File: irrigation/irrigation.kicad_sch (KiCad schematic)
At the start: 35 parts, among them J1 Power, J10 Power, J11 Power, J12 Power, J13 Power, J14 Power, J15 Power, J2 Power, J3 Power, J4 Power, J5 Power, J6 Power, J7 24V Jmp, J8 0V Jmp, J9 Power, K1 PLC-RPT-24DC/21, K2 PLC-RPT-24DC/21, M1 Pump, SW1 25% Full, SW2 50% Full, SW3 75% Full, SW4 100% Full, SW5 Well Empty, U1 MPPT-Charger

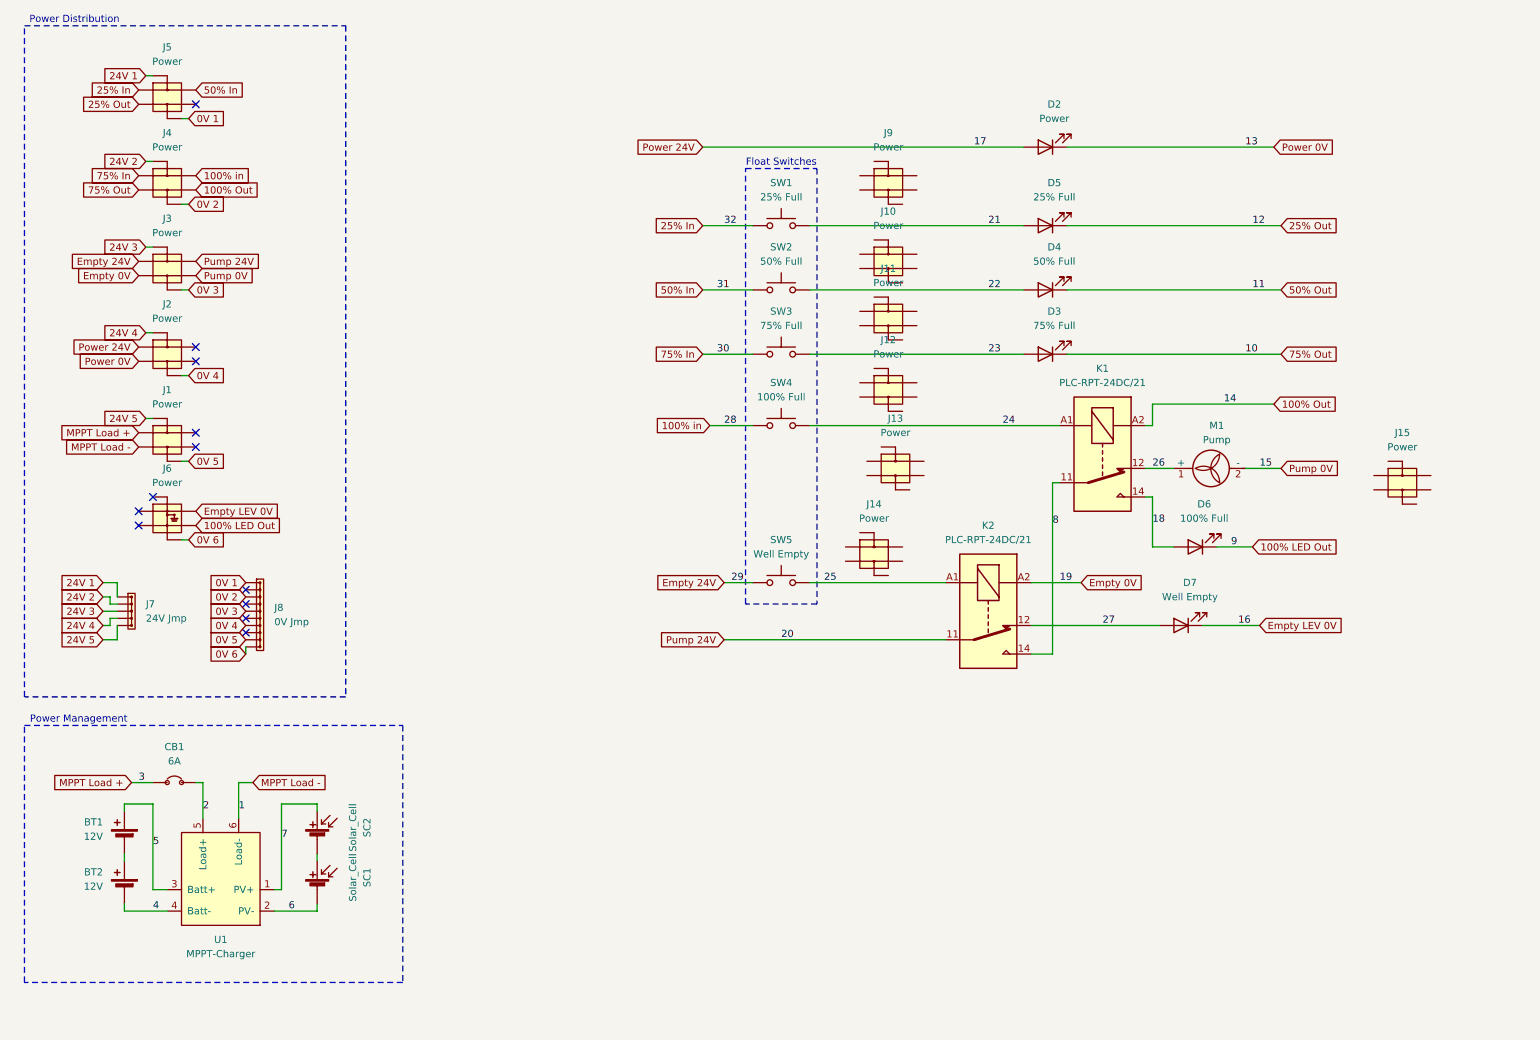
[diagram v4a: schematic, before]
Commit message: Added all the new terminal blocks
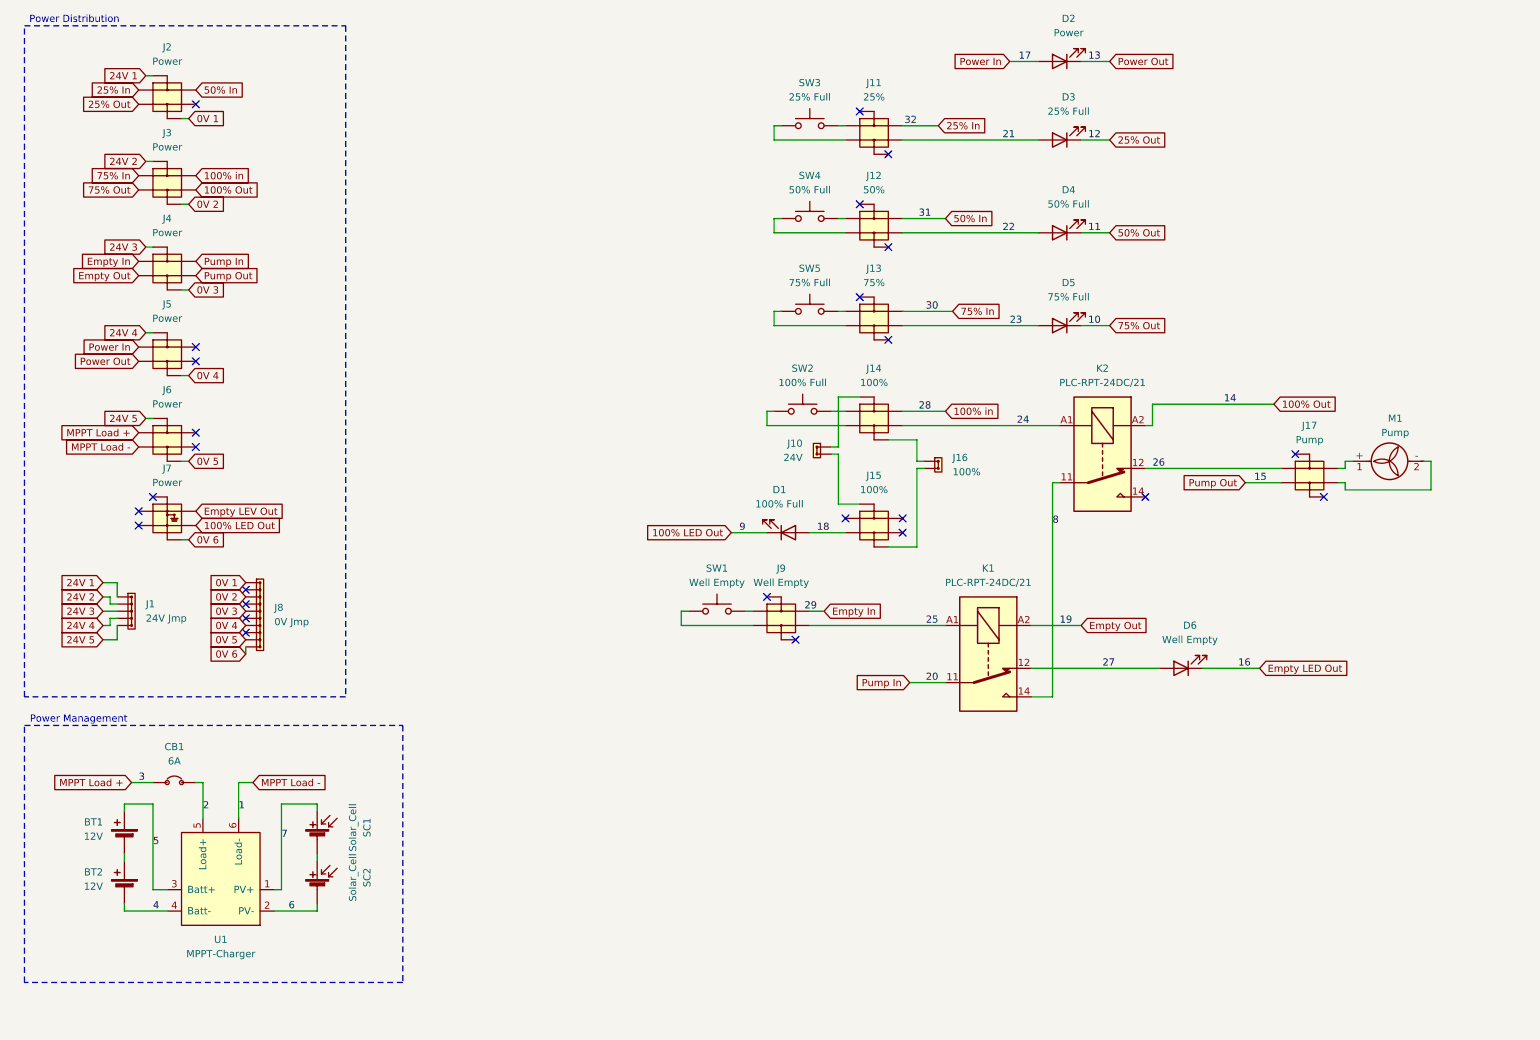
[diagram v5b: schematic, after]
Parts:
- removed J9: Power, symbol Phoenix Contact:PTTB_2,5-L/N_3210994
- added J10: 24V, symbol Phoenix Contact:FBS 2-5_3030161
- added J15: 100%, symbol Phoenix Contact:PTTB_2,5-L/N_3210994
- added J16: 100%, symbol Phoenix Contact:FBS 2-5_3030161
- J11: renamed from J10; value Power -> 25%
- J12: renamed from J11; value Power -> 50%
- J13: renamed from J12; value Power -> 75%
- J14: renamed from J13; value Power -> 100%
- J17: renamed from J15; value Power -> Pump
- J9: renamed from J14; value Power -> Well Empty
- renumbered D6 to D1, D5 to D3, D3 to D5, D7 to D6, J7 to J1, J5 to J2, J4 to J3, J3 to J4, J2 to J5, J1 to J6, J6 to J7, K2 to K1, K1 to K2, SC2 to SC1, SC1 to SC2, SW5 to SW1, SW4 to SW2, SW1 to SW3, SW2 to SW4, SW3 to SW5
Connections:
- net Power 0V is gone; now on net Power Out: D2.1 (K), J5.
- net 100% in: now also J14.; no longer SW2.1
- net 18: now also J15.; no longer K2.14
- net 21: now also J11.; no longer SW3.2
- net 22: now also J12.; no longer SW4.2
- net 23: now also J13.; no longer SW5.2
- net 24: now also J14.; no longer SW2.2
- net 25: now also J9.; no longer SW1.2
- net 25% In: now also J11.; no longer SW3.1
- net 26: now also J17.; no longer M1.1 (+)
- net 50% In: now also J12.; no longer SW4.1
- net 75% In: now also J13.; no longer SW5.1
- net Pump Out: now reaches J17.
- net Pump Out: now also J4.
- net Empty In: now reaches J9.
- net Empty In: now also J4.
- net Empty LEV Out: now reaches J7.
- net Power Out: now reaches J5.
- net Empty 0V renamed Empty Out
- net Empty 24V: no longer names the net of SW1.1
- net Empty 24V: now also J9.; no longer J4.
- net Empty LEV 0V renamed Empty LED Out
- net Empty LED Out: no longer J7.
- net Power 24V renamed Power In
- net Pump 0V: no longer names the net of M1.2 (-)
- net Pump 0V: now also J17.; no longer J4.
- net Pump 24V renamed Pump In
- new net: J13., SW5.1
- new net: J13., SW5.2
- new net: J10., J14.
- new net: J14., SW2.1
- new net: J14., SW2.2
- new net: J14., J16.
- new net: J10., J15.
- new net: J17., M1.1 (+)
- new net: J9., SW1.2
- new net: J11., SW3.1
- new net: J11., SW3.2
- new net: J12., SW4.1
- new net: J12., SW4.2
- new net: J15., J16.
- no-connect marks 12 -> 26
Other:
- note removed: "Float Switches"
- moved on the sheet: D1, D2, D3, D4, D5, D6, J11, J12, J13, J14, J17, J9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

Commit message: Attempting to organize
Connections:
- net at J10.: now also J15.; no longer J14.
- net at J16.: now also J15.; no longer J14.
- new net: J10., J14.
- new net: J14., J16.
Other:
- note added: "External Interfaces"
- moved on the sheet: D1, D2, D3, D4, D5, D6, J10, J11, J12, J13, J14, J15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

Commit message: Attempting to organize
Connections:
- net at J10.: now also J15.; no longer J14.
- net at J16.: now also J15.; no longer J14.
- new net: J10., J14.
- new net: J14., J16.
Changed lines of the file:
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@@
+	(wire
+		(pts
+			(xy 133.35 105.41) (xy 189.23 105.41)
+		)
+		(stroke
+			(width 0)
+			(type default)
+		)
+	)
 	(wire
 		(pts
@@
 	(wire
 		(pts
-			(xy 187.96 88.9) (xy 133.35 88.9)
-		)
-		(stroke
-			(width 0)
-			(type default)
-		)
-	)
-	(wire
-		(pts
 			(xy 54.61 127) (xy 54.61 128.27)
 		)
@@
 	(wire
 		(pts
+			(xy 133.35 88.9) (xy 187.96 88.9)
+		)
+		(stroke
+			(width 0)
+			(type default)
+		)
+	)
+	(wire
+		(pts
 			(xy 110.49 50.8) (xy 111.76 50.8)
 		)
@@
 	(wire
 		(pts
+			(xy 133.35 36.83) (xy 176.53 36.83)
+		)
+		(stroke
+			(width 0)
+			(type default)
+		)
+	)
+	(wire
+		(pts
 			(xy 205.74 118.11) (xy 214.63 118.11)
 		)
@@
 	(wire
 		(pts
-			(xy 189.23 105.41) (xy 133.35 105.41)
-		)
-		(stroke
-			(width 0)
-			(type default)
-		)
-	)
-	(wire
-		(pts
 			(xy 44.45 48.26) (xy 43.18 48.26)
 		)
@@
 		(pts
 			(xy 44.45 78.74) (xy 43.18 78.74)
-		)
-		(stroke
-			(width 0)
-			(type default)
-		)
-	)
-	(wire
-		(pts
-			(xy 133.35 36.83) (xy 176.53 36.83)
 		)
 		(stroke
@@
 	)
 	(label "24"
-		(at 182.88 107.95 0)
+		(at 134.62 107.95 0)
 		(effects
 			(font
@@
 	)
 	(label "31"
-		(at 138.43 50.8 180)
-		(effects
-			(font
-				(size 1.27 1.27)
-			)
-			(justify right bottom)
+		(at 134.62 50.8 0)
+		(effects
+			(font
+				(size 1.27 1.27)
+			)
+			(justify left bottom)
 		)
 	)
 	(label "26"
-		(at 137.16 86.36 0)
+		(at 134.62 86.36 0)
 		(effects
 			(font
@@
 	)
 	(label "21"
-		(at 170.18 36.83 0)
+		(at 133.35 36.83 0)
 		(effects
 			(font
@@
 	)
 	(label "29"
-		(at 135.89 140.97 180)
-		(effects
-			(font
-				(size 1.27 1.27)
-			)
-			(justify right bottom)
+		(at 134.62 140.97 0)
+		(effects
+			(font
+				(size 1.27 1.27)
+			)
+			(justify left bottom)
 		)
 	)
 	(label "23"
-		(at 171.45 69.85 0)
+		(at 134.62 69.85 0)
 		(effects
 			(font
@@
 	)
 	(label "30"
-		(at 139.7 67.31 180)
-		(effects
-			(font
-				(size 1.27 1.27)
-			)
-			(justify right bottom)
+		(at 134.62 67.31 0)
+		(effects
+			(font
+				(size 1.27 1.27)
+			)
+			(justify left bottom)
 		)
 	)
@@
 	)
 	(label "25"
-		(at 135.89 143.51 180)
-		(effects
-			(font
-				(size 1.27 1.27)
-			)
-			(justify right bottom)
+		(at 134.62 143.51 0)
+		(effects
+			(font
+				(size 1.27 1.27)
+			)
+			(justify left bottom)
 		)
 	)
@@
 	)
 	(label "22"
-		(at 170.18 53.34 0)
+		(at 134.62 53.34 0)
 		(effects
 			(font
@@
 	)
 	(label "15"
-		(at 137.16 88.9 0)
+		(at 134.62 88.9 0)
 		(effects
 			(font
@@
 	)
 	(label "18"
-		(at 170.18 124.46 180)
-		(effects
-			(font
-				(size 1.27 1.27)
-			)
-			(justify right bottom)
+		(at 134.62 124.46 0)
+		(effects
+			(font
+				(size 1.27 1.27)
+			)
+			(justify left bottom)
 		)
 	)
@@
 	)
 	(label "28"
-		(at 167.64 105.41 180)
-		(effects
-			(font
-				(size 1.27 1.27)
-			)
-			(justify right bottom)
+		(at 134.62 105.41 0)
+		(effects
+			(font
+				(size 1.27 1.27)
+			)
+			(justify left bottom)
 		)
 	)
@@
 	)
 	(label "20"
-		(at 181.61 152.4 180)
-		(effects
-			(font
+		(at 181.61 153.67 180)
+		(effects
+			(font

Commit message: Attempting to organize
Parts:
- J9: value Well Empty -> Empty
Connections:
- net at J10.: now also J15.; no longer J14.
- net at J16.: now also J15.; no longer J14.
- new net: J10., J14.
- new net: J14., J16.
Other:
- moved on the sheet: D1, D3, D4, D5, D6, J10, J11, J12, J13, J14, J15, J16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
